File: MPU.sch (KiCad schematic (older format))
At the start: 25 parts, among them J2 Conn_02x10_Counter_Clockwise, J3 Micro_SD_Card, J4 USB_A, J5 USB_A, SW1 SW_DIP_x03, U1 STM32MP151AAB3, Y1 Crystal_GND24

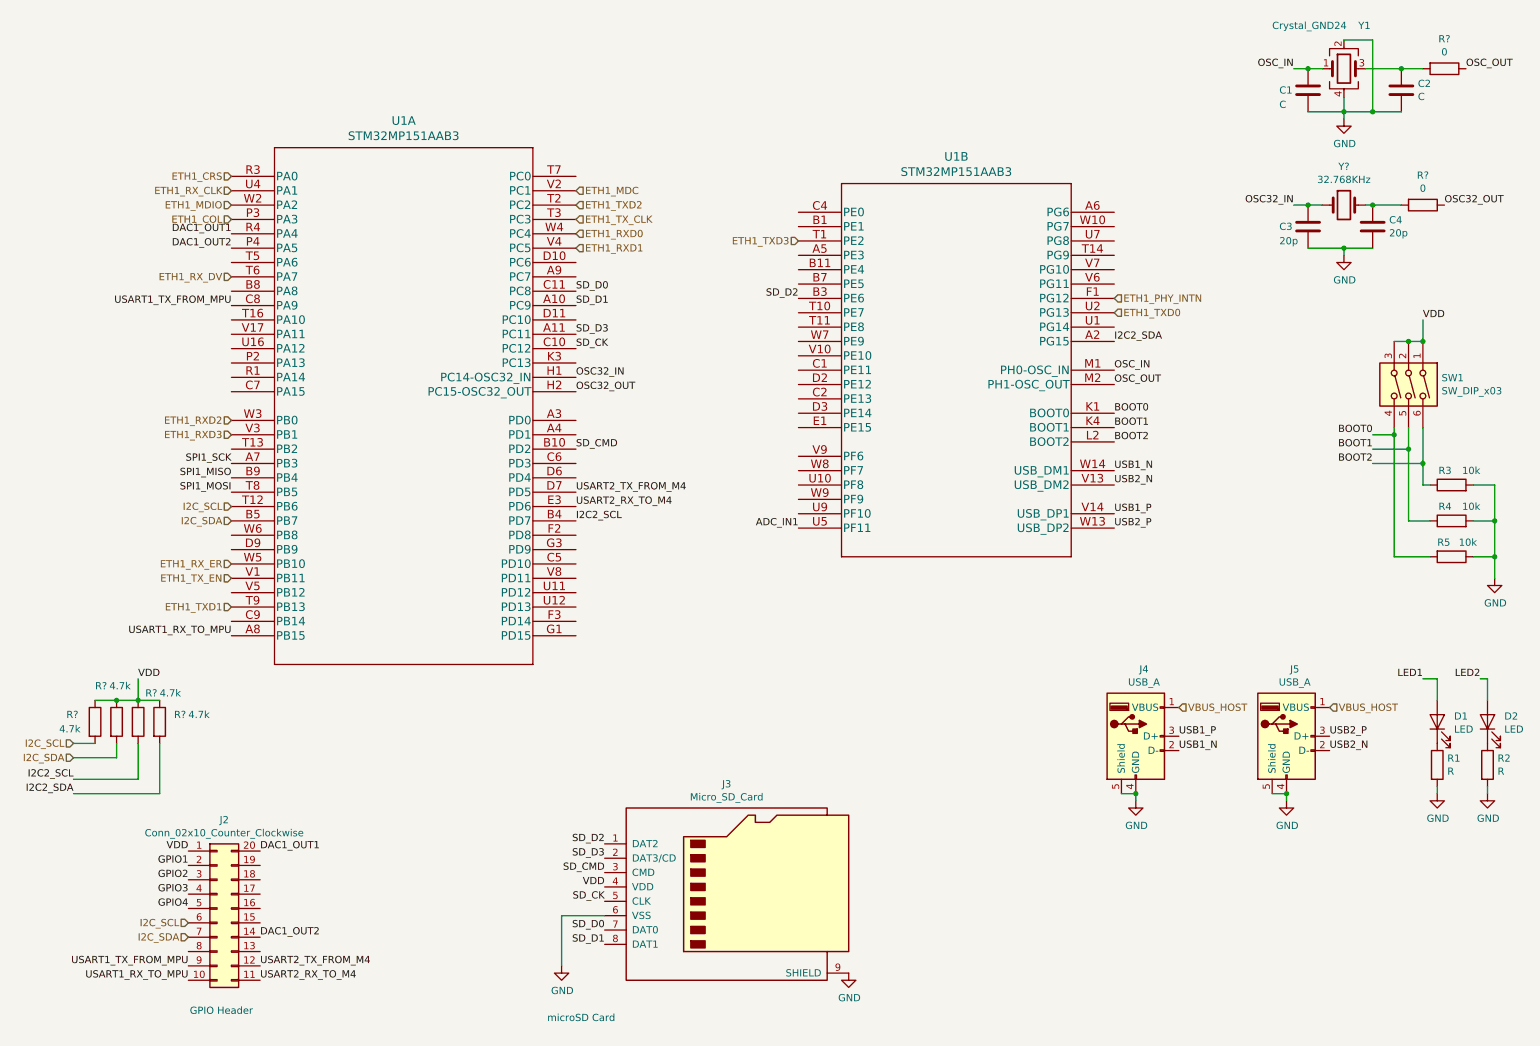
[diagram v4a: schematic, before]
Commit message: Complete gpio selection, tidy sheets
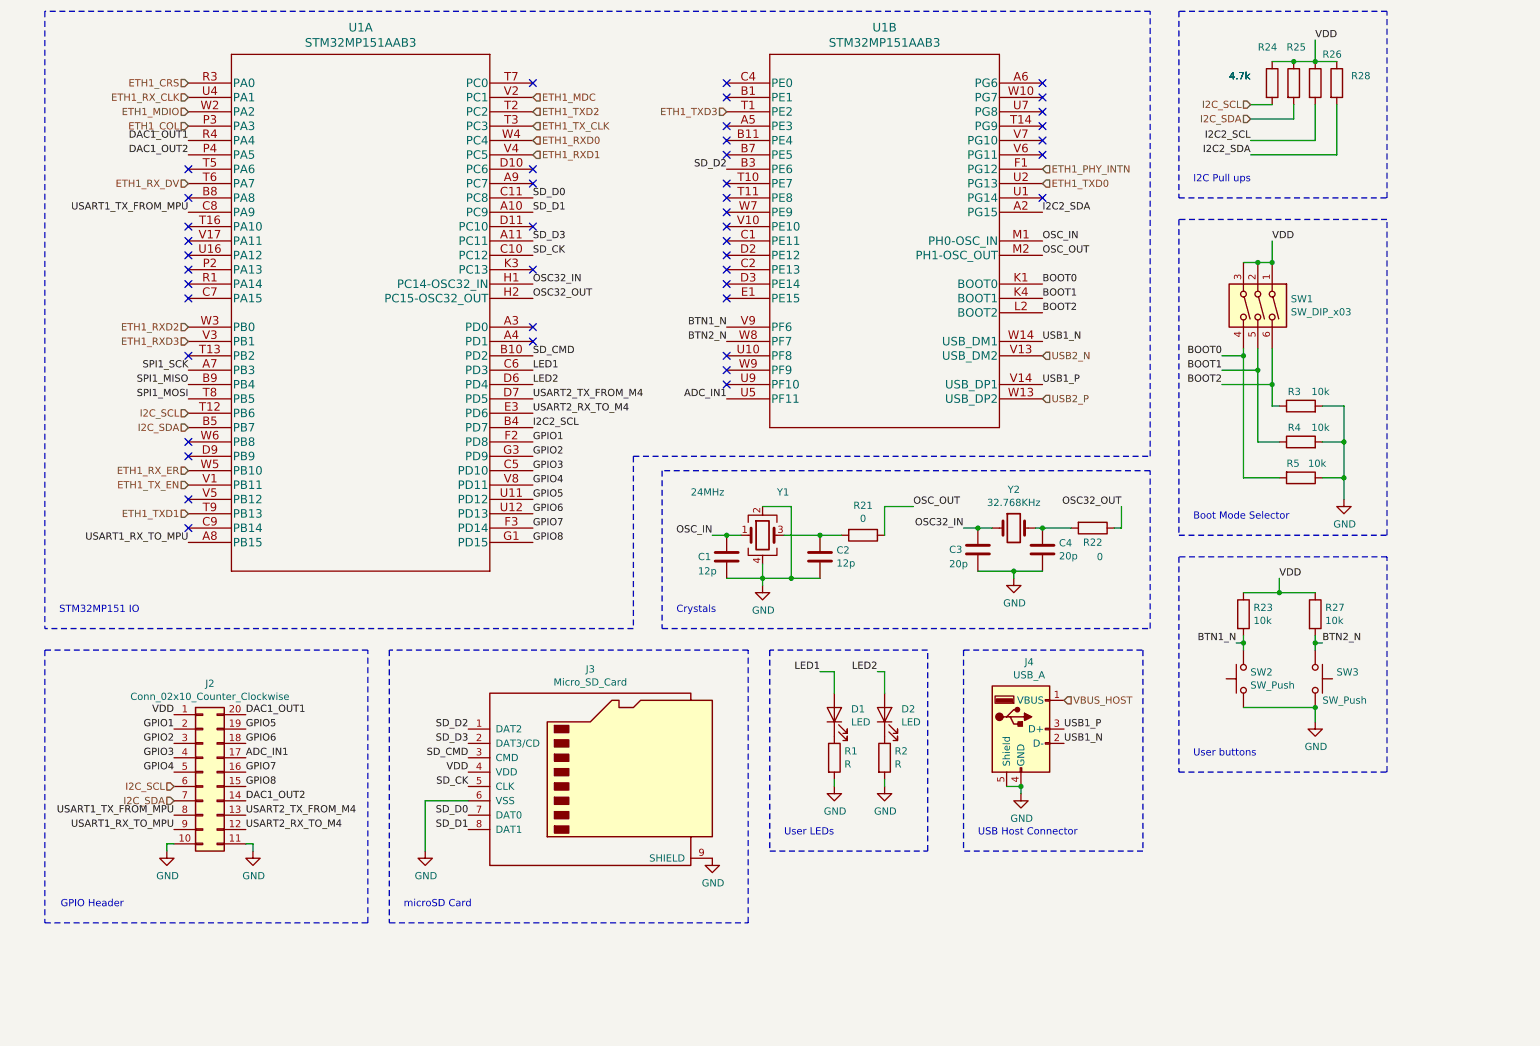
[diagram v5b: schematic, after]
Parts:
- removed J5: USB_A, Connector_USB:USB_A_CNCTech_1001-011-01101_Horizontal, symbol Connector:USB_A
- added R23, R27: 10k, symbol Device:R
- added SW2, SW3: SW_Push, symbol Switch:SW_Push
- C1, C2: value C -> 12p
- Y1: value Crystal_GND24 -> 24MHz
- gave numbers to parts that had none: 7
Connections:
- net ADC_IN1: now also J2.17 (Pin_17)
- net GND: now also J2.10 (Pin_10), J2.11 (Pin_11), SW2.1, SW3.2
- net GPIO1: now also U1.F2 (PD8)
- net GPIO2: now also U1.G3 (PD9)
- net GPIO3: now also U1.C5 (PD10)
- net GPIO4: now also U1.V8 (PD11)
- net LED1: now also U1.C6 (PD3)
- net LED2: now also U1.D6 (PD4)
- net USART1_RX_TO_MPU: now also J2.9 (Pin_9); no longer J2.10 (Pin_10)
- net USART1_TX_FROM_MPU: now also J2.8 (Pin_8); no longer J2.9 (Pin_9)
- net USART2_RX_TO_M4: now also J2.12 (Pin_12); no longer J2.11 (Pin_11)
- net USART2_TX_FROM_M4: now also J2.13 (Pin_13); no longer J2.12 (Pin_12)
- net VDD: now also R23.1, R27.1
- net GPIO7: now reaches U1.F3 (PD14)
- net GPIO7: now also J2.16 (Pin_16)
- net GPIO8: now reaches U1.G1 (PD15)
- net GPIO8: now also J2.15 (Pin_15)
- net GPIO5: now reaches U1.U11 (PD12)
- net GPIO5: now also J2.19 (Pin_19)
- net GPIO6: now reaches U1.U12 (PD13)
- net GPIO6: now also J2.18 (Pin_18)
- net BTN1_N: now reaches U1.V9 (PF6)
- net BTN1_N: now also R23.2, SW2.2
- net BTN2_N: now reaches U1.W8 (PF7)
- net BTN2_N: now also R27.2, SW3.1
- no-connect marks 0 -> 44
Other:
- note added: "Boot Mode Selector"
- note added: "Crystals"
- note added: "I2C Pull ups\n"
- note added: "STM32MP151 IO"
- note added: "USB Host Connector"
- note added: "User LEDs\n"
- note added: "User buttons\n"
- moved on the sheet: C1, C2, C3, C4, D1, D2, J2, J3, J4, R1, R2, R21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

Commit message: Start crossing off ERC. Add generated BOM
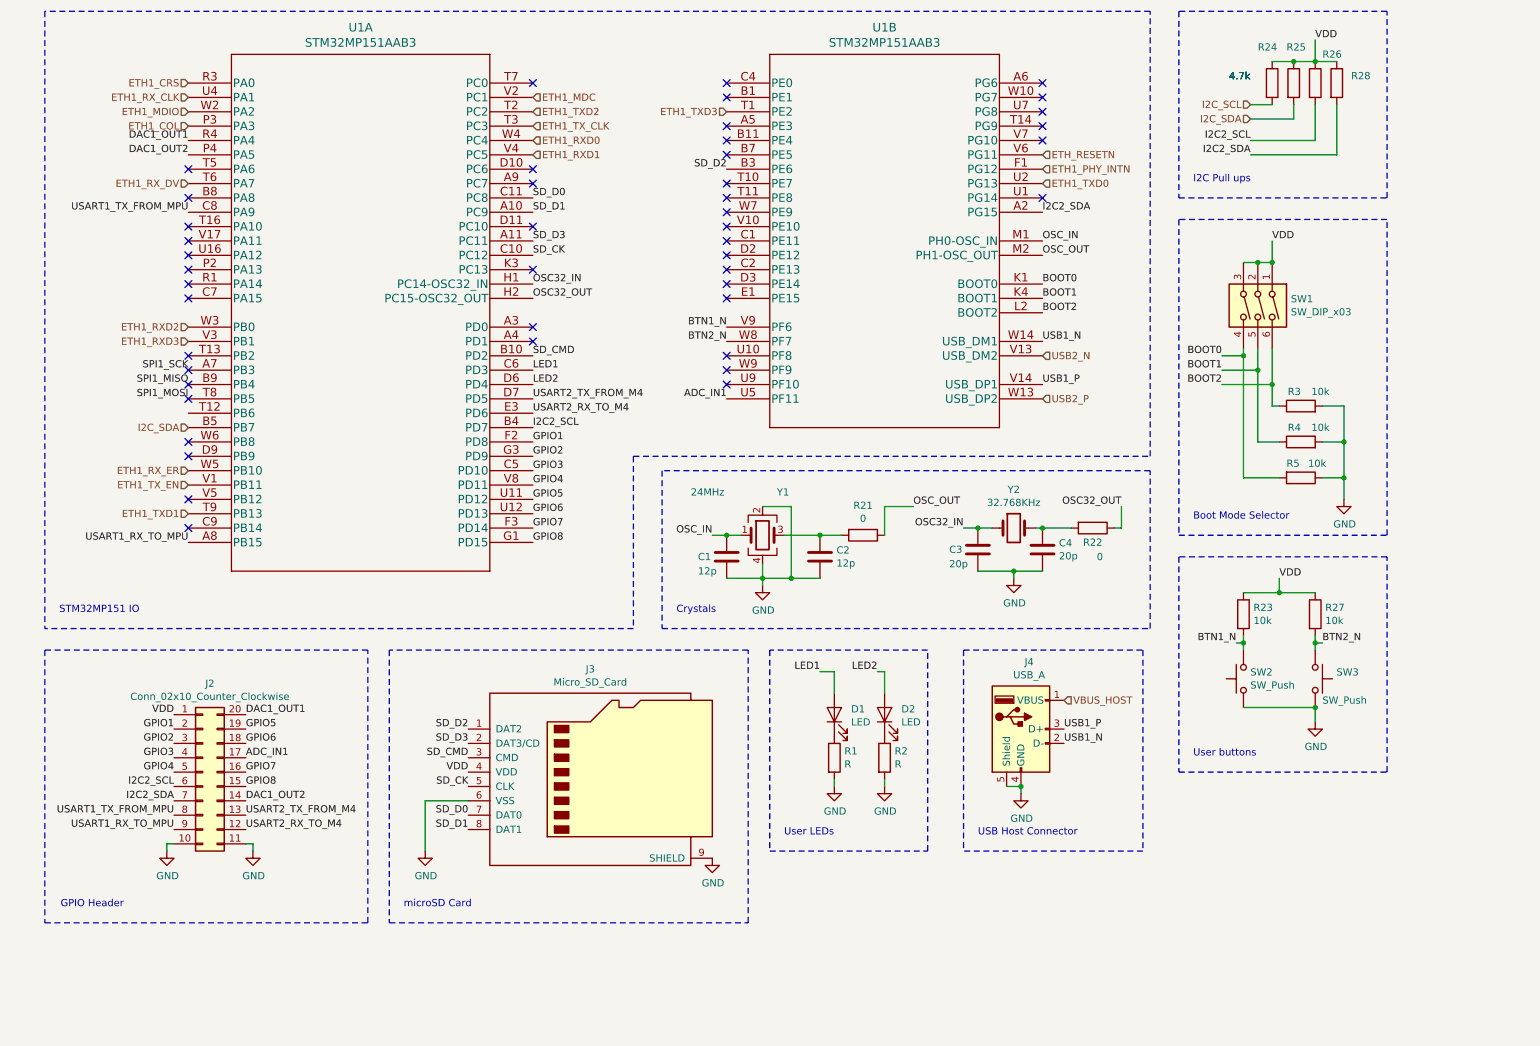
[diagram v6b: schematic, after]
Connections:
- net I2C2_SCL: now also J2.6 (Pin_6)
- net I2C2_SDA: now also J2.7 (Pin_7)
- net I2C_SCL: no longer J2.6 (Pin_6), U1.T12 (PB6)
- net I2C_SDA: no longer J2.7 (Pin_7)
- net ETH_RESETN: now reaches U1.V6 (PG11)
- no-connect marks 44 -> 46

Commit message: Complete schematic rough draft
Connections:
- net PMIC_INT_N: now reaches U1.K3 (PC13)
- net PMIC_WAKEUP: now reaches U1.D2 (PE12)
- no-connect marks 46 -> 45
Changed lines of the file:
@@
 NoConn ~ 4150 2850
 NoConn ~ 4150 2750
-NoConn ~ 4150 2350
 NoConn ~ 4150 2050
 NoConn ~ 4150 1650
@@
 NoConn ~ 5500 1850
 NoConn ~ 5500 1950
-NoConn ~ 5500 2050
-NoConn ~ 5500 2150
-NoConn ~ 5500 2250
 NoConn ~ 5500 2350
 NoConn ~ 5500 2550
@@
 Text Label 1650 5550 2    50   ~ 0
 GPIO1
-Text Label 3700 5850 2    50   ~ 0
-VDD
 Text Label 7850 5650 0    50   ~ 0
 USB1_N
@@
 Wire Wire Line
 	9100 5000 9100 4950
-Text Label 9350 4500 0    50   ~ 0
-VDD
 Wire Wire Line
 	9350 4600 9600 4600
@@
 Wire Wire Line
 	9300 2150 9300 2300
-Text Label 9300 2150 0    50   ~ 0
-VDD
 Wire Wire Line
 	9650 3300 9800 3300
@@
 Text Notes 8750 1750 0    50   ~ 0
 I2C Pull ups\n
-Wire Wire Line
-	9600 750  9600 900
-Text Label 9600 750  0    50   ~ 0
-VDD
 Wire Wire Line
 	9600 900  9750 900
@@
 Text Label 4150 3950 0    50   ~ 0
 GPIO5
+NoConn ~ 1750 3350
+Text HLabel 3700 5850 0    50   Input ~ 0
+VDD
+Text HLabel 9350 4500 0    50   Input ~ 0
+VDD
+Text HLabel 9300 2150 0    50   Input ~ 0
+VDD
+Text HLabel 9600 700  0    50   Input ~ 0
+VDD
+Wire Wire Line
+	9600 700  9600 900
+Text HLabel 4150 2350 2    50   Input ~ 0
+PMIC_INT_N
+Text HLabel 5500 2250 0    50   Input ~ 0
+PMIC_WAKEUP
+NoConn ~ 5500 2050
+NoConn ~ 5500 2150
 $EndSCHEMATC

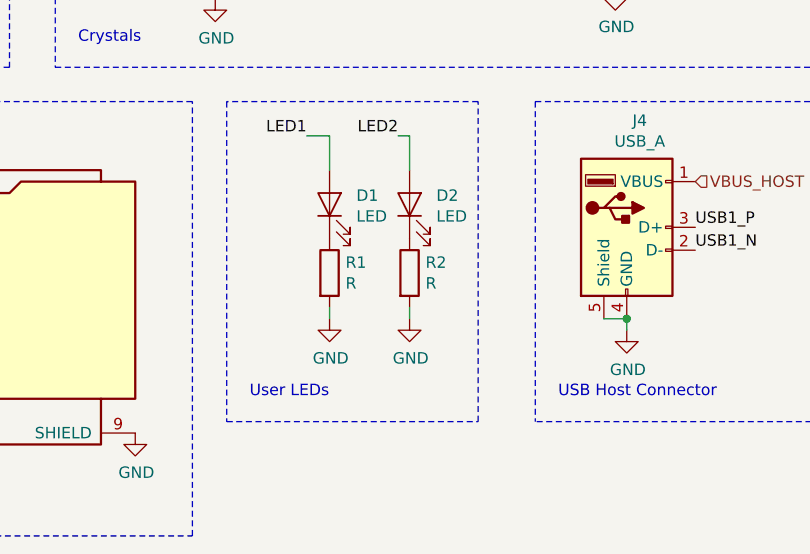
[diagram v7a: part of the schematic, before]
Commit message: Update footprints
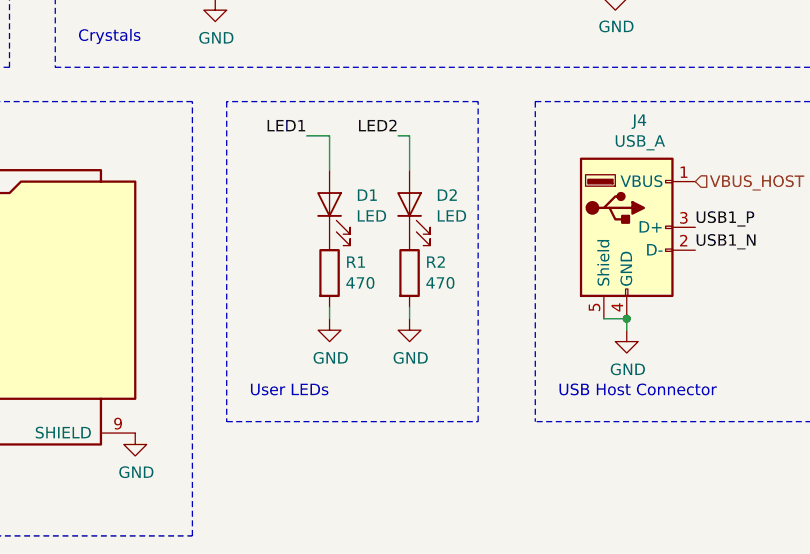
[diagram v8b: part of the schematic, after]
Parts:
- R1, R2: value R -> 470; footprint Resistor_SMD:R_0603_1608Metric -> Resistor_SMD:R_0603_1608Metric_Pad1.05x0.95mm_HandSolder
- R21, R22, R23, R24, R25, R26, R27, R28: footprint (none) -> Resistor_SMD:R_0603_1608Metric_Pad1.05x0.95mm_HandSolder
- R3, R4, R5: footprint Resistor_SMD:R_0603_1608Metric -> Resistor_SMD:R_0603_1608Metric_Pad1.05x0.95mm_HandSolder
- SW2, SW3: footprint (none) -> Button_Switch_SMD:SW_Push_1P1T_NO_6x6mm_H9.5mm
- Y1: footprint Crystal:Crystal_SMD_2520-4Pin_2.5x2.0mm -> Crystal:Crystal_SMD_2016-4Pin_2.0x1.6mm
- Y2: footprint (none) -> Crystal:Crystal_SMD_TXC_9HT11-2Pin_2.0x1.2mm
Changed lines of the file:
@@
 F 0 "Y1" H 5850 4500 50  0000 L CNN
 F 1 "24MHz" H 5250 4500 50  0000 L CNN
-F 2 "Crystal:Crystal_SMD_2520-4Pin_2.5x2.0mm" H 5750 4200 50  0001 C CNN
+F 2 "Crystal:Crystal_SMD_2016-4Pin_2.0x1.6mm" H 5750 4200 50  0001 C CNN
 F 3 "~" H 5750 4200 50  0001 C CNN
 	1    5750 4200
@@
 F 0 "R21" V 6243 4200 50  0000 C CNN
 F 1 "0" V 6334 4200 50  0000 C CNN
-F 2 "" V 6380 4200 50  0001 C CNN
+F 2 "Resistor_SMD:R_0603_1608Metric_Pad1.05x0.95mm_HandSolder" V 6380 4200 50  0001 C CNN
 F 3 "~" H 6450 4200 50  0001 C CNN
 	1    6450 4200
@@
 F 0 "R22" V 8150 4150 50  0000 C CNN
 F 1 "0" V 8250 4200 50  0000 C CNN
-F 2 "" V 7980 4150 50  0001 C CNN
+F 2 "Resistor_SMD:R_0603_1608Metric_Pad1.05x0.95mm_HandSolder" V 7980 4150 50  0001 C CNN
 F 3 "~" H 8050 4150 50  0001 C CNN
 	1    8050 4150
@@
 F 0 "Y2" H 7500 4418 50  0000 C CNN
 F 1 "32.768KHz" H 7500 4327 50  0000 C CNN
-F 2 "" H 7500 4150 50  0001 C CNN
+F 2 "Crystal:Crystal_SMD_TXC_9HT11-2Pin_2.0x1.2mm" H 7500 4150 50  0001 C CNN
 F 3 "~" H 7500 4150 50  0001 C CNN
 	1    7500 4150
@@
 AR Path="/601728C0/60644ED5" Ref="R2"  Part="1"
 F 0 "R2" H 6670 5796 50  0000 L CNN
-F 1 "R" H 6670 5705 50  0000 L CNN
-F 2 "Resistor_SMD:R_0603_1608Metric" V 6530 5750 50  0001 C CNN
+F 1 "470" H 6670 5705 50  0000 L CNN
+F 2 "Resistor_SMD:R_0603_1608Metric_Pad1.05x0.95mm_HandSolder" V 6530 5750 50  0001 C CNN
 F 3 "~" H 6600 5750 50  0001 C CNN
 	1    6600 5750
@@
 AR Path="/601728C0/60642C91" Ref="R1"  Part="1"
 F 0 "R1" H 6320 5796 50  0000 L CNN
-F 1 "R" H 6320 5705 50  0000 L CNN
-F 2 "Resistor_SMD:R_0603_1608Metric" V 6180 5750 50  0001 C CNN
+F 1 "470" H 6320 5705 50  0000 L CNN
+F 2 "Resistor_SMD:R_0603_1608Metric_Pad1.05x0.95mm_HandSolder" V 6180 5750 50  0001 C CNN
 F 3 "~" H 6250 5750 50  0001 C CNN
 	1    6250 5750
@@
 F 0 "R27" H 9670 4796 50  0000 L CNN
 F 1 "10k" H 9670 4705 50  0000 L CNN
-F 2 "" V 9530 4750 50  0001 C CNN
+F 2 "Resistor_SMD:R_0603_1608Metric_Pad1.05x0.95mm_HandSolder" V 9530 4750 50  0001 C CNN
 F 3 "~" H 9600 4750 50  0001 C CNN
 	1    9600 4750
@@
 F 0 "R23" H 9170 4796 50  0000 L CNN
 F 1 "10k" H 9170 4705 50  0000 L CNN
-F 2 "" V 9030 4750 50  0001 C CNN
+F 2 "Resistor_SMD:R_0603_1608Metric_Pad1.05x0.95mm_HandSolder" V 9030 4750 50  0001 C CNN
 F 3 "~" H 9100 4750 50  0001 C CNN
 	1    9100 4750
@@
 F 0 "SW2" V 9146 5152 50  0000 R CNN
 F 1 "SW_Push" V 9055 5152 50  0000 R CNN
-F 2 "" H 9100 5400 50  0001 C CNN
+F 2 "Button_Switch_SMD:SW_Push_1P1T_NO_6x6mm_H9.5mm" H 9100 5400 50  0001 C CNN
 F 3 "~" H 9100 5400 50  0001 C CNN
 	1    9100 5200
@@
 F 0 "SW3" V 9554 5348 50  0000 L CNN
 F 1 "SW_Push" V 9750 5250 50  0000 L CNN
-F 2 "" H 9600 5400 50  0001 C CNN
+F 2 "Button_Switch_SMD:SW_Push_1P1T_NO_6x6mm_H9.5mm" H 9600 5400 50  0001 C CNN
 F 3 "~" H 9600 5400 50  0001 C CNN
 	1    9600 5200
@@
 F 0 "R3" V 9600 3300 50  0000 L CNN
 F 1 "10k" V 9600 3100 50  0000 L CNN
-F 2 "Resistor_SMD:R_0603_1608Metric" V 9430 3300 50  0001 C CNN
+F 2 "Resistor_SMD:R_0603_1608Metric_Pad1.05x0.95mm_HandSolder" V 9430 3300 50  0001 C CNN
 F 3 "~" H 9500 3300 50  0001 C CNN
 	1    9500 3300
@@
 F 0 "R4" V 9600 3550 50  0000 L CNN
 F 1 "10k" V 9600 3350 50  0000 L CNN
-F 2 "Resistor_SMD:R_0603_1608Metric" V 9430 3550 50  0001 C CNN
+F 2 "Resistor_SMD:R_0603_1608Metric_Pad1.05x0.95mm_HandSolder" V 9430 3550 50  0001 C CNN
 F 3 "~" H 9500 3550 50  0001 C CNN
 	1    9500 3550
@@
 F 0 "R5" V 9400 3700 50  0000 L CNN
 F 1 "10k" V 9400 3850 50  0000 L CNN
-F 2 "Resistor_SMD:R_0603_1608Metric" V 9430 3800 50  0001 C CNN
+F 2 "Resistor_SMD:R_0603_1608Metric_Pad1.05x0.95mm_HandSolder" V 9430 3800 50  0001 C CNN
 F 3 "~" H 9500 3800 50  0001 C CNN
 	1    9500 3800
@@
 F 0 "R28" H 9850 1100 50  0000 L CNN
 F 1 "4.7k" H 9000 1100 50  0000 L CNN
-F 2 "" V 9680 1050 50  0001 C CNN
+F 2 "Resistor_SMD:R_0603_1608Metric_Pad1.05x0.95mm_HandSolder" V 9680 1050 50  0001 C CNN
 F 3 "~" H 9750 1050 50  0001 C CNN
 	1    9750 1050
@@
 F 0 "R26" H 9650 1250 50  0000 L CNN
 F 1 "4.7k" H 9000 1100 50  0000 L CNN
-F 2 "" V 9530 1050 50  0001 C CNN
+F 2 "Resistor_SMD:R_0603_1608Metric_Pad1.05x0.95mm_HandSolder" V 9530 1050 50  0001 C CNN
 F 3 "~" H 9600 1050 50  0001 C CNN
 	1    9600 1050
@@
 F 0 "R25" H 9400 1300 50  0000 L CNN
 F 1 "4.7k" H 9000 1100 50  0000 L CNN
-F 2 "" V 9380 1050 50  0001 C CNN
+F 2 "Resistor_SMD:R_0603_1608Metric_Pad1.05x0.95mm_HandSolder" V 9380 1050 50  0001 C CNN
 F 3 "~" H 9450 1050 50  0001 C CNN
 	1    9450 1050
@@
 F 0 "R24" H 9200 1300 50  0000 L CNN
 F 1 "4.7k" H 9000 1100 50  0000 L CNN
-F 2 "" V 9230 1050 50  0001 C CNN
+F 2 "Resistor_SMD:R_0603_1608Metric_Pad1.05x0.95mm_HandSolder" V 9230 1050 50  0001 C CNN
 F 3 "~" H 9300 1050 50  0001 C CNN
 	1    9300 1050
